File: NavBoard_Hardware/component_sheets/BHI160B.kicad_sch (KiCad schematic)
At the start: 12 parts, among them U2 BHI160B

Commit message: Updated sheet title info
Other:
- company: Missouri S&T Rover Design Team -> Thomas Francois, Katherine Dunlap, Missouri S&T Mars Rover Design Team
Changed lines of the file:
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@@
     (date "2022-09-15")
     (rev "2, 2023")
-    (company "Missouri S&T Rover Design Team")
+    (company "Thomas Francois, Katherine Dunlap, Missouri S&T Mars Rover Design Team")
     (comment 1 "BHI160B IMU & Supporting Components")
     (comment 2 "Provides Position & Acceleration Data")

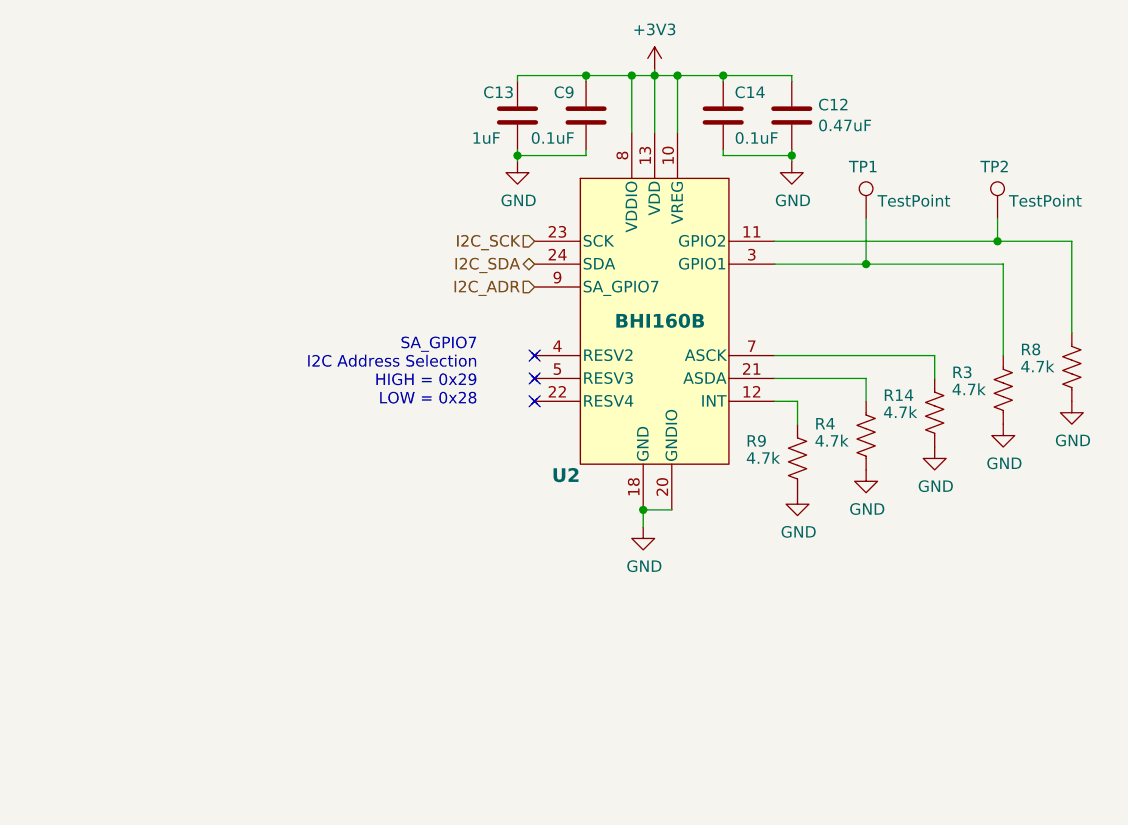
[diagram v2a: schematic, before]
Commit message: Corrected accelerometer regulator capacitors
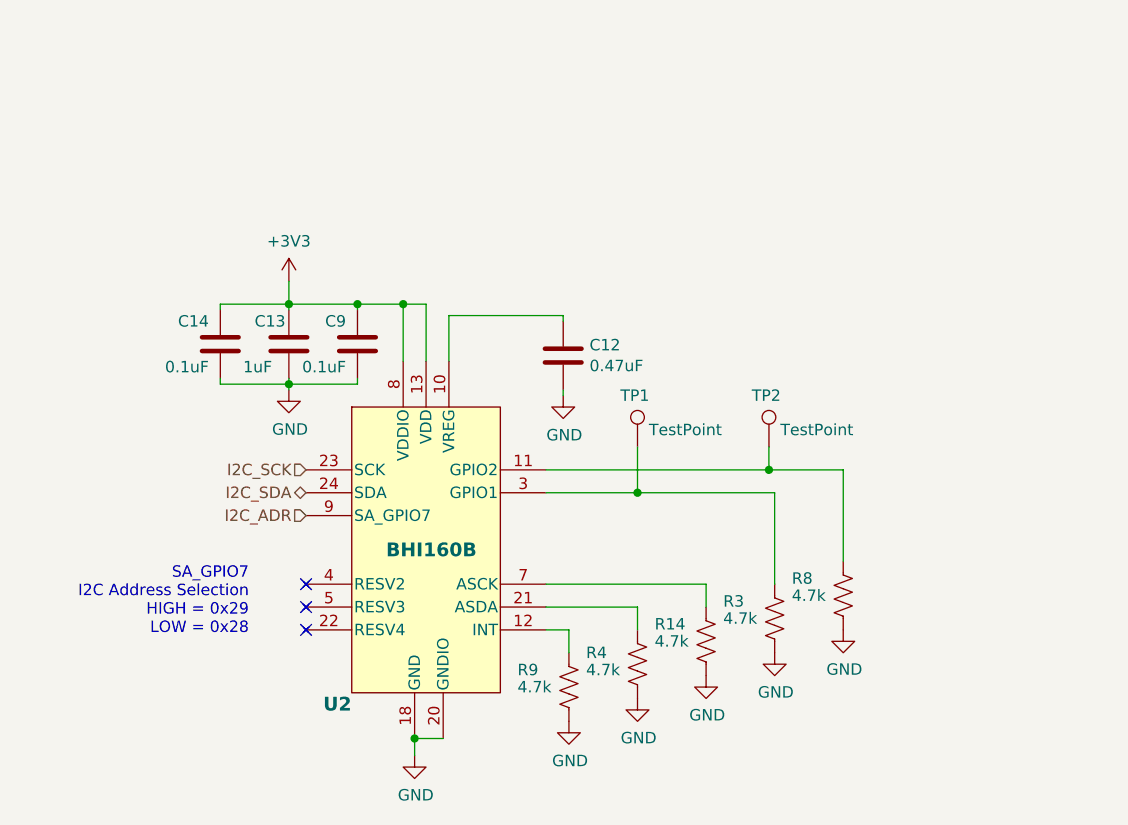
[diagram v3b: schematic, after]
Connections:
- net +3V3: no longer C12.1, U2.10 (VREG)
- new net: C12.1, U2.10 (VREG)
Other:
- moved on the sheet: C12, C13, C14, C9, R14, R3, R4, R8, R9, TP1, TP2, U2

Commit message: Most schematic connections completed
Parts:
- U1: renamed from U2; footprint BHI160B:BHI160B -> LGA24_3X3X0P95_3_BOS
- renumbered C13 to C1, C9 to C2, C14 to C3, C12 to C4, R9 to R1, R4 to R2, R14 to R3, R3 to R4, R8 to R5
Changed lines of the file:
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@@
   (symbol (lib_id "Device:R_US") (at 191.135 106.045 0) (unit 1)
     (in_bom yes) (on_board yes)
-    (property "Reference" "R3" (id 0) (at 185.42 104.14 0)
+    (property "Reference" "R4" (id 0) (at 185.42 104.14 0)
       (effects (font (size 1.27 1.27)) (justify left))
     )
@@
   (symbol (lib_id "Device:R_US") (at 183.515 108.585 0) (unit 1)
     (in_bom yes) (on_board yes)
-    (property "Reference" "R14" (id 0) (at 177.8 106.68 0)
+    (property "Reference" "R3" (id 0) (at 177.8 106.68 0)
       (effects (font (size 1.27 1.27)) (justify left))
     )
@@
   (symbol (lib_id "power:GND") (at 151.13 121.285 0) (unit 1)
     (in_bom yes) (on_board yes)
-    (property "Reference" "#PWR0109" (id 0) (at 151.13 127.635 0)
+    (property "Reference" "#PWR02" (id 0) (at 151.13 127.635 0)
       (effects (font (size 1.27 1.27)) hide)
     )
@@
   (symbol (lib_id "power:GND") (at 175.895 114.935 0) (unit 1)
     (in_bom yes) (on_board yes)
-    (property "Reference" "#PWR013" (id 0) (at 175.895 121.285 0)
+    (property "Reference" "#PWR06" (id 0) (at 175.895 121.285 0)
       (effects (font (size 1.27 1.27)) hide)
     )
@@
   (symbol (lib_id "Device:R_US") (at 198.755 103.505 0) (unit 1)
     (in_bom yes) (on_board yes)
-    (property "Reference" "R8" (id 0) (at 193.04 101.6 0)
+    (property "Reference" "R5" (id 0) (at 193.04 101.6 0)
       (effects (font (size 1.27 1.27)) (justify left))
     )
@@
   (symbol (lib_id "power:GND") (at 167.64 81.28 0) (unit 1)
     (in_bom yes) (on_board yes)
-    (property "Reference" "#PWR06" (id 0) (at 167.64 87.63 0)
+    (property "Reference" "#PWR04" (id 0) (at 167.64 87.63 0)
       (effects (font (size 1.27 1.27)) hide)
     )
@@
   (symbol (lib_id "power:GND") (at 191.135 109.855 0) (unit 1)
     (in_bom yes) (on_board yes)
-    (property "Reference" "#PWR021" (id 0) (at 191.135 116.205 0)
+    (property "Reference" "#PWR08" (id 0) (at 191.135 116.205 0)
       (effects (font (size 1.27 1.27)) hide)
     )
@@
   (symbol (lib_id "Device:C") (at 167.64 76.835 0) (unit 1)
     (in_bom yes) (on_board yes)
-    (property "Reference" "C12" (id 0) (at 170.561 75.6666 0)
+    (property "Reference" "C4" (id 0) (at 170.561 75.6666 0)
       (effects (font (size 1.27 1.27)) (justify left))
     )
@@
   (symbol (lib_id "MRDT_Sensors:BHI160B") (at 152.4 97.155 0) (unit 1)
     (in_bom yes) (on_board yes)
-    (property "Reference" "U2" (id 0) (at 140.97 115.57 0)
+    (property "Reference" "U1" (id 0) (at 140.97 115.57 0)
       (effects (font (size 1.524 1.524) bold) (justify left))
     )
@@
       (effects (font (size 1.524 1.524) bold) (justify left))
     )
-    (property "Footprint" "BHI160B:BHI160B" (id 2) (at 154.305 72.39 0)
+    (property "Footprint" "LGA24_3X3X0P95_3_BOS" (id 2) (at 154.305 72.39 0)
       (effects (font (size 1.524 1.524)) hide)
     )
@@
   (symbol (lib_id "Device:R_US") (at 168.275 113.665 0) (unit 1)
     (in_bom yes) (on_board yes)
-    (property "Reference" "R9" (id 0) (at 162.56 111.76 0)
+    (property "Reference" "R1" (id 0) (at 162.56 111.76 0)
       (effects (font (size 1.27 1.27)) (justify left))
     )
@@
   (symbol (lib_id "power:+3V3") (at 137.16 68.58 0) (unit 1)
     (in_bom yes) (on_board yes)
-    (property "Reference" "#PWR05" (id 0) (at 137.16 72.39 0)
+    (property "Reference" "#PWR03" (id 0) (at 137.16 72.39 0)
       (effects (font (size 1.27 1.27)) hide)
     )
@@
   (symbol (lib_id "power:GND") (at 198.755 107.315 0) (unit 1)
     (in_bom yes) (on_board yes)
-    (property "Reference" "#PWR023" (id 0) (at 198.755 113.665 0)
+    (property "Reference" "#PWR09" (id 0) (at 198.755 113.665 0)
       (effects (font (size 1.27 1.27)) hide)
     )
@@
   (symbol (lib_id "Device:C") (at 144.78 75.565 0) (mirror y) (unit 1)
     (in_bom yes) (on_board yes)
-    (property "Reference" "C9" (id 0) (at 143.51 73.025 0)
+    (property "Reference" "C2" (id 0) (at 143.51 73.025 0)
       (effects (font (size 1.27 1.27)) (justify left))
     )
@@
   (symbol (lib_id "power:GND") (at 183.515 112.395 0) (unit 1)
     (in_bom yes) (on_board yes)
-    (property "Reference" "#PWR020" (id 0) (at 183.515 118.745 0)
+    (property "Reference" "#PWR07" (id 0) (at 183.515 118.745 0)
       (effects (font (size 1.27 1.27)) hide)
     )
@@
   (symbol (lib_id "Device:C") (at 129.54 75.565 0) (mirror y) (unit 1)
     (in_bom yes) (on_board yes)
-    (property "Reference" "C14" (id 0) (at 128.27 73.025 0)
+    (property "Reference" "C3" (id 0) (at 128.27 73.025 0)
       (effects (font (size 1.27 1.27)) (justify left))
     )
@@
   (symbol (lib_id "Device:R_US") (at 175.895 111.125 0) (unit 1)
     (in_bom yes) (on_board yes)
-    (property "Reference" "R4" (id 0) (at 170.18 109.855 0)
+    (property "Reference" "R2" (id 0) (at 170.18 109.855 0)
       (effects (font (size 1.27 1.27)) (justify left))
     )
@@
   (symbol (lib_id "Device:C") (at 137.16 75.565 0) (unit 1)
     (in_bom yes) (on_board yes)
-    (property "Reference" "C13" (id 0) (at 133.35 73.025 0)
+    (property "Reference" "C1" (id 0) (at 133.35 73.025 0)
       (effects (font (size 1.27 1.27)) (justify left))
     )
@@
   (symbol (lib_id "power:GND") (at 168.275 117.475 0) (unit 1)
     (in_bom yes) (on_board yes)
-    (property "Reference" "#PWR012" (id 0) (at 168.275 123.825 0)
-      (effects (font (size 1.27 1.27)) hide)
-    )
+    (property "Reference" "#PWR05" (id 0) (at 168.275 123.825 0)
+      (effects (font (size 1.27 1.27)) hide)
+    )

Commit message: Annotated Schematic, assigned footprints, recovered accelerometer footprints
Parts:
- U1: footprint LGA24_3X3X0P95_3_BOS -> Nav_Board:BHI160B
- renumbered C3 to C1, C1 to C2, C2 to C3, R5 to R1, R4 to R2, R2 to R4, R1 to R5
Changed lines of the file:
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@@
   (symbol (lib_id "Device:R_US") (at 191.135 106.045 0) (unit 1)
     (in_bom yes) (on_board yes)
-    (property "Reference" "R4" (id 0) (at 185.42 104.14 0)
+    (property "Reference" "R2" (id 0) (at 185.42 104.14 0)
       (effects (font (size 1.27 1.27)) (justify left))
     )
@@
   (symbol (lib_id "power:GND") (at 151.13 121.285 0) (unit 1)
     (in_bom yes) (on_board yes)
-    (property "Reference" "#PWR02" (id 0) (at 151.13 127.635 0)
+    (property "Reference" "#PWR09" (id 0) (at 151.13 127.635 0)
       (effects (font (size 1.27 1.27)) hide)
     )
@@
   (symbol (lib_id "power:GND") (at 175.895 114.935 0) (unit 1)
     (in_bom yes) (on_board yes)
-    (property "Reference" "#PWR06" (id 0) (at 175.895 121.285 0)
+    (property "Reference" "#PWR07" (id 0) (at 175.895 121.285 0)
       (effects (font (size 1.27 1.27)) hide)
     )
@@
   (symbol (lib_id "Device:R_US") (at 198.755 103.505 0) (unit 1)
     (in_bom yes) (on_board yes)
-    (property "Reference" "R5" (id 0) (at 193.04 101.6 0)
+    (property "Reference" "R1" (id 0) (at 193.04 101.6 0)
       (effects (font (size 1.27 1.27)) (justify left))
     )
@@
   (symbol (lib_id "power:GND") (at 137.16 80.645 0) (unit 1)
     (in_bom yes) (on_board yes)
-    (property "Reference" "#PWR01" (id 0) (at 137.16 86.995 0)
+    (property "Reference" "#PWR02" (id 0) (at 137.16 86.995 0)
       (effects (font (size 1.27 1.27)) hide)
     )
@@
   (symbol (lib_id "power:GND") (at 167.64 81.28 0) (unit 1)
     (in_bom yes) (on_board yes)
-    (property "Reference" "#PWR04" (id 0) (at 167.64 87.63 0)
+    (property "Reference" "#PWR03" (id 0) (at 167.64 87.63 0)
       (effects (font (size 1.27 1.27)) hide)
     )
@@
   (symbol (lib_id "power:GND") (at 191.135 109.855 0) (unit 1)
     (in_bom yes) (on_board yes)
-    (property "Reference" "#PWR08" (id 0) (at 191.135 116.205 0)
+    (property "Reference" "#PWR05" (id 0) (at 191.135 116.205 0)
       (effects (font (size 1.27 1.27)) hide)
     )
@@
       (effects (font (size 1.524 1.524) bold) (justify left))
     )
-    (property "Footprint" "LGA24_3X3X0P95_3_BOS" (id 2) (at 154.305 72.39 0)
+    (property "Footprint" "Nav_Board:BHI160B" (id 2) (at 154.305 72.39 0)
       (effects (font (size 1.524 1.524)) hide)
     )
@@
   (symbol (lib_id "Device:R_US") (at 168.275 113.665 0) (unit 1)
     (in_bom yes) (on_board yes)
-    (property "Reference" "R1" (id 0) (at 162.56 111.76 0)
+    (property "Reference" "R5" (id 0) (at 162.56 111.76 0)
       (effects (font (size 1.27 1.27)) (justify left))
     )
@@
   (symbol (lib_id "power:+3V3") (at 137.16 68.58 0) (unit 1)
     (in_bom yes) (on_board yes)
-    (property "Reference" "#PWR03" (id 0) (at 137.16 72.39 0)
+    (property "Reference" "#PWR01" (id 0) (at 137.16 72.39 0)
       (effects (font (size 1.27 1.27)) hide)
     )
@@
   (symbol (lib_id "power:GND") (at 198.755 107.315 0) (unit 1)
     (in_bom yes) (on_board yes)
-    (property "Reference" "#PWR09" (id 0) (at 198.755 113.665 0)
+    (property "Reference" "#PWR04" (id 0) (at 198.755 113.665 0)
       (effects (font (size 1.27 1.27)) hide)
     )
@@
   (symbol (lib_id "Device:C") (at 144.78 75.565 0) (mirror y) (unit 1)
     (in_bom yes) (on_board yes)
-    (property "Reference" "C2" (id 0) (at 143.51 73.025 0)
+    (property "Reference" "C3" (id 0) (at 143.51 73.025 0)
       (effects (font (size 1.27 1.27)) (justify left))
     )
@@
   (symbol (lib_id "power:GND") (at 183.515 112.395 0) (unit 1)
     (in_bom yes) (on_board yes)
-    (property "Reference" "#PWR07" (id 0) (at 183.515 118.745 0)
+    (property "Reference" "#PWR06" (id 0) (at 183.515 118.745 0)
       (effects (font (size 1.27 1.27)) hide)
     )
@@
   (symbol (lib_id "Device:C") (at 129.54 75.565 0) (mirror y) (unit 1)
     (in_bom yes) (on_board yes)
-    (property "Reference" "C3" (id 0) (at 128.27 73.025 0)
+    (property "Reference" "C1" (id 0) (at 128.27 73.025 0)
       (effects (font (size 1.27 1.27)) (justify left))
     )
@@
   (symbol (lib_id "Device:R_US") (at 175.895 111.125 0) (unit 1)
     (in_bom yes) (on_board yes)
-    (property "Reference" "R2" (id 0) (at 170.18 109.855 0)
+    (property "Reference" "R4" (id 0) (at 170.18 109.855 0)
       (effects (font (size 1.27 1.27)) (justify left))
     )
@@
   (symbol (lib_id "Device:C") (at 137.16 75.565 0) (unit 1)
     (in_bom yes) (on_board yes)
-    (property "Reference" "C1" (id 0) (at 133.35 73.025 0)
+    (property "Reference" "C2" (id 0) (at 133.35 73.025 0)
       (effects (font (size 1.27 1.27)) (justify left))
     )
@@
   (symbol (lib_id "power:GND") (at 168.275 117.475 0) (unit 1)
     (in_bom yes) (on_board yes)
-    (property "Reference" "#PWR05" (id 0) (at 168.275 123.825 0)
-      (effects (font (size 1.27 1.27)) hide)
-    )
+    (property "Reference" "#PWR08" (id 0) (at 168.275 123.825 0)
+      (effects (font (size 1.27 1.27)) hide)
+    )

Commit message: Completed routing, added 3D models to IMUs
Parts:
- TP1, TP2: footprint TestPoint:TestPoint_Pad_D2.0mm -> TestPoint:TestPoint_Pad_D1.5mm
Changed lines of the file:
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@@
       (effects (font (size 1.27 1.27)) (justify left))
     )
-    (property "Footprint" "TestPoint:TestPoint_Pad_D2.0mm" (id 2) (at 195.58 86.995 0)
+    (property "Footprint" "TestPoint:TestPoint_Pad_D1.5mm" (id 2) (at 195.58 86.995 0)
       (effects (font (size 1.27 1.27)) hide)
     )
@@
       (effects (font (size 1.27 1.27)) (justify left))
     )
-    (property "Footprint" "TestPoint:TestPoint_Pad_D2.0mm" (id 2) (at 180.975 86.995 0)
+    (property "Footprint" "TestPoint:TestPoint_Pad_D1.5mm" (id 2) (at 180.975 86.995 0)
       (effects (font (size 1.27 1.27)) hide)
     )

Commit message: Annotated schematic pages
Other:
- company: Thomas Francois, Katherine Dunlap, Missouri S&T Mars Rover Design Team -> Thomas Francois, Missouri S&T Mars Rover Design Team
- title: BHI160B Inertial Measurement Unit -> MRDT NavBoard - BHI160B
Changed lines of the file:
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@@
   (paper "A4")
   (title_block
-    (title "BHI160B Inertial Measurement Unit")
+    (title "MRDT NavBoard - BHI160B")
     (date "2022-09-15")
-    (rev "2, 2023")
-    (company "Thomas Francois, Katherine Dunlap, Missouri S&T Mars Rover Design Team")
-    (comment 1 "BHI160B IMU & Supporting Components")
-    (comment 2 "Provides Position & Acceleration Data")
+    (rev "1, 2023")
+    (company "Thomas Francois, Missouri S&T Mars Rover Design Team")
+    (comment 1 "BHI160B Inertial Measurement Unit & Supporting Components")
+    (comment 2 "Provides Position and Acceleration Data")
   )
   (junction (at 190.5 89.535) (diameter 0) (color 0 0 0 0)

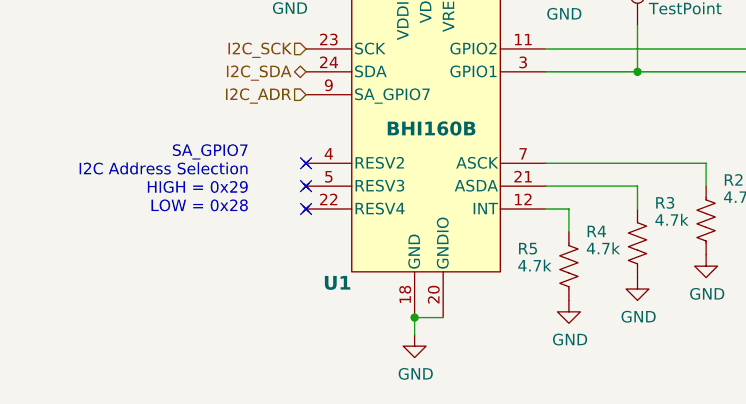
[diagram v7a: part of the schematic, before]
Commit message: Realized this could all fit on a single board
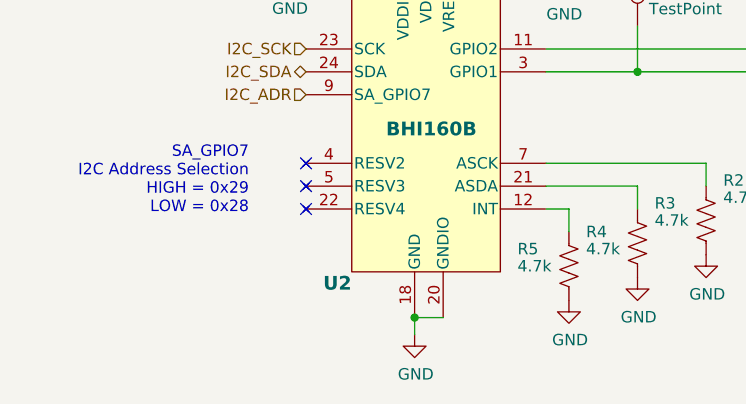
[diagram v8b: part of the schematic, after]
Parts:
- renumbered U1 to U2
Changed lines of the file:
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@@
   (symbol (lib_id "power:GND") (at 151.13 121.285 0) (unit 1)
     (in_bom yes) (on_board yes)
-    (property "Reference" "#PWR09" (id 0) (at 151.13 127.635 0)
+    (property "Reference" "#PWR020" (id 0) (at 151.13 127.635 0)
       (effects (font (size 1.27 1.27)) hide)
     )
@@
   (symbol (lib_id "power:GND") (at 175.895 114.935 0) (unit 1)
     (in_bom yes) (on_board yes)
-    (property "Reference" "#PWR07" (id 0) (at 175.895 121.285 0)
+    (property "Reference" "#PWR018" (id 0) (at 175.895 121.285 0)
       (effects (font (size 1.27 1.27)) hide)
     )
@@
   (symbol (lib_id "power:GND") (at 137.16 80.645 0) (unit 1)
     (in_bom yes) (on_board yes)
-    (property "Reference" "#PWR02" (id 0) (at 137.16 86.995 0)
+    (property "Reference" "#PWR013" (id 0) (at 137.16 86.995 0)
       (effects (font (size 1.27 1.27)) hide)
     )
@@
   (symbol (lib_id "power:GND") (at 167.64 81.28 0) (unit 1)
     (in_bom yes) (on_board yes)
-    (property "Reference" "#PWR03" (id 0) (at 167.64 87.63 0)
+    (property "Reference" "#PWR014" (id 0) (at 167.64 87.63 0)
       (effects (font (size 1.27 1.27)) hide)
     )
@@
   (symbol (lib_id "power:GND") (at 191.135 109.855 0) (unit 1)
     (in_bom yes) (on_board yes)
-    (property "Reference" "#PWR05" (id 0) (at 191.135 116.205 0)
+    (property "Reference" "#PWR016" (id 0) (at 191.135 116.205 0)
       (effects (font (size 1.27 1.27)) hide)
     )
@@
   (symbol (lib_id "MRDT_Sensors:BHI160B") (at 152.4 97.155 0) (unit 1)
     (in_bom yes) (on_board yes)
-    (property "Reference" "U1" (id 0) (at 140.97 115.57 0)
+    (property "Reference" "U2" (id 0) (at 140.97 115.57 0)
       (effects (font (size 1.524 1.524) bold) (justify left))
     )
@@
   (symbol (lib_id "power:+3V3") (at 137.16 68.58 0) (unit 1)
     (in_bom yes) (on_board yes)
-    (property "Reference" "#PWR01" (id 0) (at 137.16 72.39 0)
+    (property "Reference" "#PWR012" (id 0) (at 137.16 72.39 0)
       (effects (font (size 1.27 1.27)) hide)
     )
@@
   (symbol (lib_id "power:GND") (at 198.755 107.315 0) (unit 1)
     (in_bom yes) (on_board yes)
-    (property "Reference" "#PWR04" (id 0) (at 198.755 113.665 0)
+    (property "Reference" "#PWR015" (id 0) (at 198.755 113.665 0)
       (effects (font (size 1.27 1.27)) hide)
     )
@@
   (symbol (lib_id "power:GND") (at 183.515 112.395 0) (unit 1)
     (in_bom yes) (on_board yes)
-    (property "Reference" "#PWR06" (id 0) (at 183.515 118.745 0)
+    (property "Reference" "#PWR017" (id 0) (at 183.515 118.745 0)
       (effects (font (size 1.27 1.27)) hide)
     )
@@
   (symbol (lib_id "power:GND") (at 168.275 117.475 0) (unit 1)
     (in_bom yes) (on_board yes)
-    (property "Reference" "#PWR08" (id 0) (at 168.275 123.825 0)
-      (effects (font (size 1.27 1.27)) hide)
-    )
+    (property "Reference" "#PWR019" (id 0) (at 168.275 123.825 0)
+      (effects (font (size 1.27 1.27)) hide)
+    )
